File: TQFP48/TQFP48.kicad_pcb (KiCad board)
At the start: 2 copper layers, 61.2 x 18 mm, 11 parts, among them J1 Conn_01x24, J2 Conn_02x24_Counter_Clockwise, J3 Conn_02x24_Counter_Clockwise, J4 Conn_01x24, J5 Conn_01x05

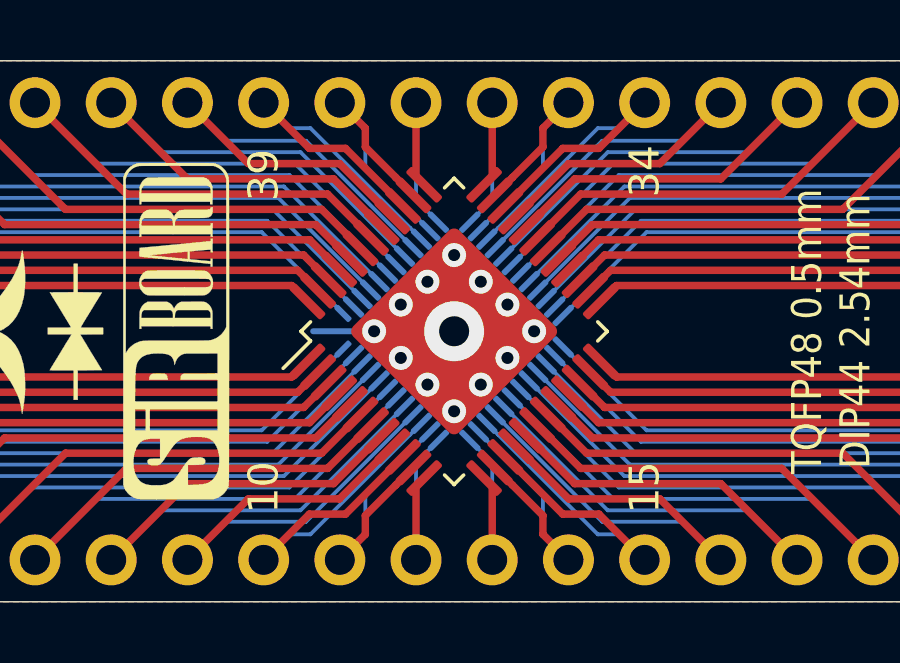
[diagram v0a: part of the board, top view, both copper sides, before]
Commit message: Silkscreens and sizes updated
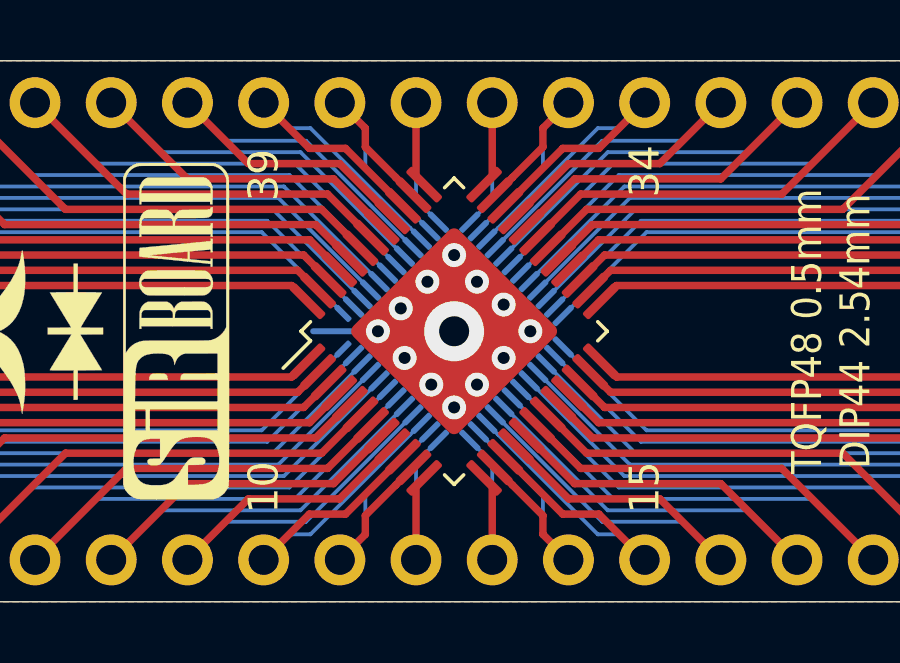
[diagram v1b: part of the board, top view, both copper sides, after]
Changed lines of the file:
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@@
   (page A4)
   (layers
-    (0 F.Cu signal hide)
-    (31 B.Cu signal hide)
+    (0 F.Cu signal)
+    (31 B.Cu signal)
     (32 B.Adhes user hide)
     (33 F.Adhes user hide)
@@
     (35 F.Paste user hide)
     (36 B.SilkS user)
-    (37 F.SilkS user hide)
-    (38 B.Mask user)
+    (37 F.SilkS user)
+    (38 B.Mask user hide)
     (39 F.Mask user hide)
     (40 Dwgs.User user hide)
@@
   )
   (module Package_QFP:TQFP-48-1EP_7x7mm_P0.5mm_EP5x5mm (layer F.Cu)
-    (at 148.59 104.145117 45)
+    (at 148.59 104.14 45)
     (descr "TQFP, 48 Pin (https://www.trinamic.com/fileadmin/assets/Products/ICs_Documents/TMC2100_datasheet_Rev1.08.pdf (page 45)), generated with kicad-footprint-generator ipc_qfp_generator.py")
     (tags "TQFP QFP")
@@
     (effects (font (size 1 1) (thickness 0.15)))
   )
-  (gr_circle (center 149.479833 102.49) (end 149.78 102.49) (layer B.Mask) (width 0.2))
-  (gr_circle (center 149.48 102.49) (end 149.780167 102.49) (layer F.Mask) (width 0.2))
-  (gr_circle (center 150.369833 103.25) (end 150.67 103.25) (layer B.Mask) (width 0.2))
-  (gr_circle (center 150.37 103.25) (end 150.670167 103.25) (layer F.Mask) (width 0.2))
-  (gr_circle (center 151.259833 104.14) (end 151.56 104.14) (layer B.Mask) (width 0.2))
-  (gr_circle (center 151.26 104.14) (end 151.560167 104.14) (layer F.Mask) (width 0.2))
-  (gr_circle (center 150.369833 105.03) (end 150.67 105.03) (layer B.Mask) (width 0.2))
-  (gr_circle (center 150.37 105.03) (end 150.670167 105.03) (layer F.Mask) (width 0.2))
-  (gr_circle (center 149.479833 105.92) (end 149.78 105.92) (layer B.Mask) (width 0.2))
-  (gr_circle (center 149.48 105.92) (end 149.780167 105.92) (layer F.Mask) (width 0.2))
-  (gr_circle (center 148.589833 106.81) (end 148.89 106.81) (layer B.Mask) (width 0.2))
-  (gr_circle (center 148.59 106.81) (end 148.890167 106.81) (layer F.Mask) (width 0.2))
-  (gr_circle (center 147.699833 105.92) (end 148 105.92) (layer B.Mask) (width 0.2))
-  (gr_circle (center 147.7 105.92) (end 148.000167 105.92) (layer F.Mask) (width 0.2))
-  (gr_circle (center 146.809833 105.03) (end 147.11 105.03) (layer B.Mask) (width 0.2))
-  (gr_circle (center 146.81 105.03) (end 147.110167 105.03) (layer F.Mask) (width 0.2))
-  (gr_circle (center 145.919833 104.14) (end 146.22 104.14) (layer B.Mask) (width 0.2))
-  (gr_circle (center 145.92 104.14) (end 146.220167 104.14) (layer F.Mask) (width 0.2))
-  (gr_circle (center 146.809833 103.25) (end 147.11 103.25) (layer B.Mask) (width 0.2))
-  (gr_circle (center 146.81 103.25) (end 147.110167 103.25) (layer F.Mask) (width 0.2))
+  (gr_circle (center 149.352 102.49) (end 149.652167 102.49) (layer B.Mask) (width 0.2))
+  (gr_circle (center 149.352 102.489) (end 149.652167 102.489) (layer F.Mask) (width 0.2))
+  (gr_circle (center 150.241 103.251) (end 150.541167 103.251) (layer B.Mask) (width 0.2))
+  (gr_circle (center 150.241 103.251) (end 150.541167 103.251) (layer F.Mask) (width 0.2))
+  (gr_circle (center 151.13 104.14) (end 151.430167 104.14) (layer B.Mask) (width 0.2))
+  (gr_circle (center 151.13 104.14) (end 151.430167 104.14) (layer F.Mask) (width 0.2))
+  (gr_circle (center 150.241 105.03) (end 150.541167 105.03) (layer B.Mask) (width 0.2))
+  (gr_circle (center 150.241 105.03) (end 150.541167 105.03) (layer F.Mask) (width 0.2))
+  (gr_circle (center 149.352 105.918) (end 149.652167 105.918) (layer B.Mask) (width 0.2))
+  (gr_circle (center 149.352 105.92) (end 149.652167 105.92) (layer F.Mask) (width 0.2))
+  (gr_circle (center 148.59 106.68) (end 148.890167 106.68) (layer B.Mask) (width 0.2))
+  (gr_circle (center 148.59 106.68) (end 148.890167 106.68) (layer F.Mask) (width 0.2))
+  (gr_circle (center 147.828 105.92) (end 148.128167 105.92) (layer B.Mask) (width 0.2))
+  (gr_circle (center 147.828 105.918) (end 148.128167 105.918) (layer F.Mask) (width 0.2))
+  (gr_circle (center 146.939 105.029) (end 147.239167 105.029) (layer B.Mask) (width 0.2))
+  (gr_circle (center 146.939 105.029) (end 147.239167 105.029) (layer F.Mask) (width 0.2))
+  (gr_circle (center 146.05 104.14) (end 146.350167 104.14) (layer B.Mask) (width 0.2))
+  (gr_circle (center 146.05 104.14) (end 146.350167 104.14) (layer F.Mask) (width 0.2))
+  (gr_circle (center 146.809833 103.378) (end 147.11 103.378) (layer B.Mask) (width 0.2))
+  (gr_circle (center 146.81 103.378) (end 147.110167 103.378) (layer F.Mask) (width 0.2))
   (gr_circle (center 147.699833 102.49) (end 148 102.49) (layer B.Mask) (width 0.2))
   (gr_circle (center 147.7 102.49) (end 148.000167 102.49) (layer F.Mask) (width 0.2))
@@
   (segment (start 173.482 100.838) (end 176.674151 97.645849) (width 0.127) (layer B.Cu) (net 48))
   (via (at 148.59 104.14) (size 2) (drill 1) (layers F.Cu B.Cu) (net 49))
-  (via (at 145.923 104.14) (size 0.8) (drill 0.4) (layers F.Cu B.Cu) (net 49))
-  (via (at 146.812 103.251) (size 0.8) (drill 0.4) (layers F.Cu B.Cu) (net 49))
-  (via (at 146.812 105.029) (size 0.8) (drill 0.4) (layers F.Cu B.Cu) (net 49))
-  (via (at 150.368 105.029) (size 0.8) (drill 0.4) (layers F.Cu B.Cu) (net 49))
-  (via (at 150.368 103.251) (size 0.8) (drill 0.4) (layers F.Cu B.Cu) (net 49))
+  (via (at 146.05 104.14) (size 0.8) (drill 0.4) (layers F.Cu B.Cu) (net 49))
+  (via (at 146.812 103.378) (size 0.8) (drill 0.4) (layers F.Cu B.Cu) (net 49))
+  (via (at 146.939 105.029) (size 0.8) (drill 0.4) (layers F.Cu B.Cu) (net 49))
+  (via (at 150.241 105.029) (size 0.8) (drill 0.4) (layers F.Cu B.Cu) (net 49))
+  (via (at 150.241 103.251) (size 0.8) (drill 0.4) (layers F.Cu B.Cu) (net 49))
   (via (at 147.701 102.489) (size 0.8) (drill 0.4) (layers F.Cu B.Cu) (net 49))
-  (via (at 149.479 102.489) (size 0.8) (drill 0.4) (layers F.Cu B.Cu) (net 49))
-  (via (at 147.701 105.918) (size 0.8) (drill 0.4) (layers F.Cu B.Cu) (net 49))
-  (via (at 149.479 105.918) (size 0.8) (drill 0.4) (layers F.Cu B.Cu) (net 49))
-  (via (at 148.59 106.807) (size 0.8) (drill 0.4) (layers F.Cu B.Cu) (net 49))
+  (via (at 149.352 102.489) (size 0.8) (drill 0.4) (layers F.Cu B.Cu) (net 49))
+  (via (at 147.828 105.918) (size 0.8) (drill 0.4) (layers F.Cu B.Cu) (net 49))
+  (via (at 149.352 105.918) (size 0.8) (drill 0.4) (layers F.Cu B.Cu) (net 49))
+  (via (at 148.59 106.68) (size 0.8) (drill 0.4) (layers F.Cu B.Cu) (net 49))
   (via (at 148.59 101.6) (size 0.8) (drill 0.4) (layers F.Cu B.Cu) (net 49))
-  (via (at 151.257 104.14) (size 0.8) (drill 0.4) (layers F.Cu B.Cu) (net 49))
+  (via (at 151.13 104.14) (size 0.8) (drill 0.4) (layers F.Cu B.Cu) (net 49))
   (segment (start 148.59 104.14) (end 143.891 104.14) (width 0.2) (layer B.Cu) (net 49))
   (zone (net 49) (net_name "Net-(J5-Pad1)") (layer B.Cu) (hatch none 0.508)

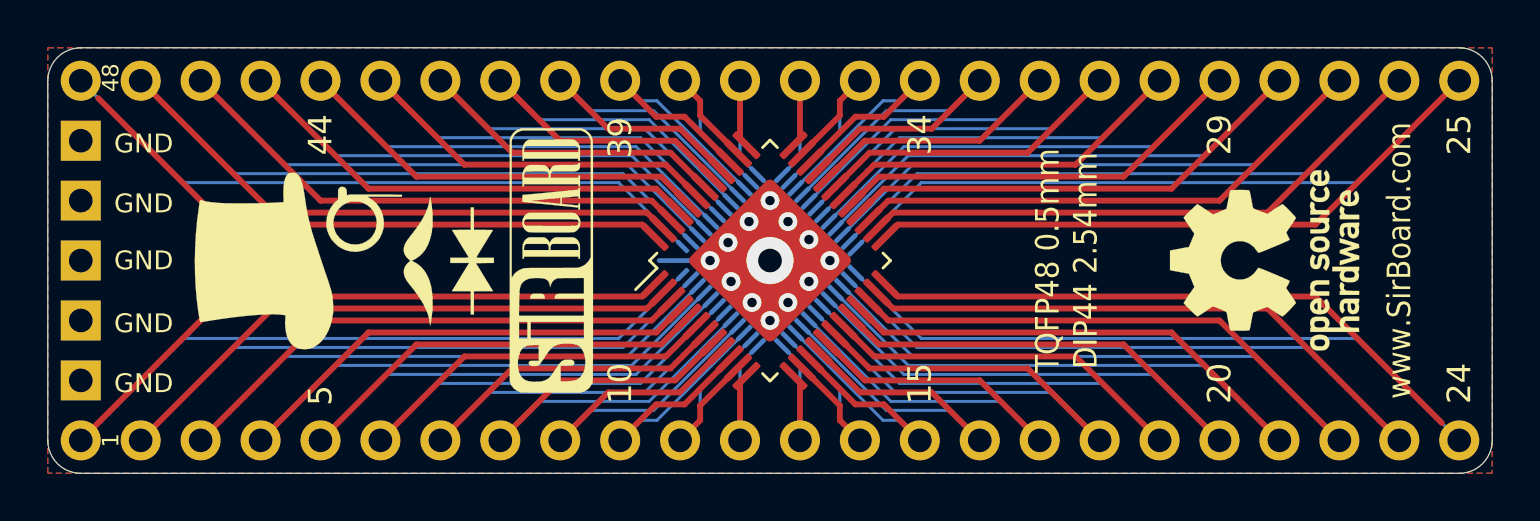
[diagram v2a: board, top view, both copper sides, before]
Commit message: Pin Numbering edited
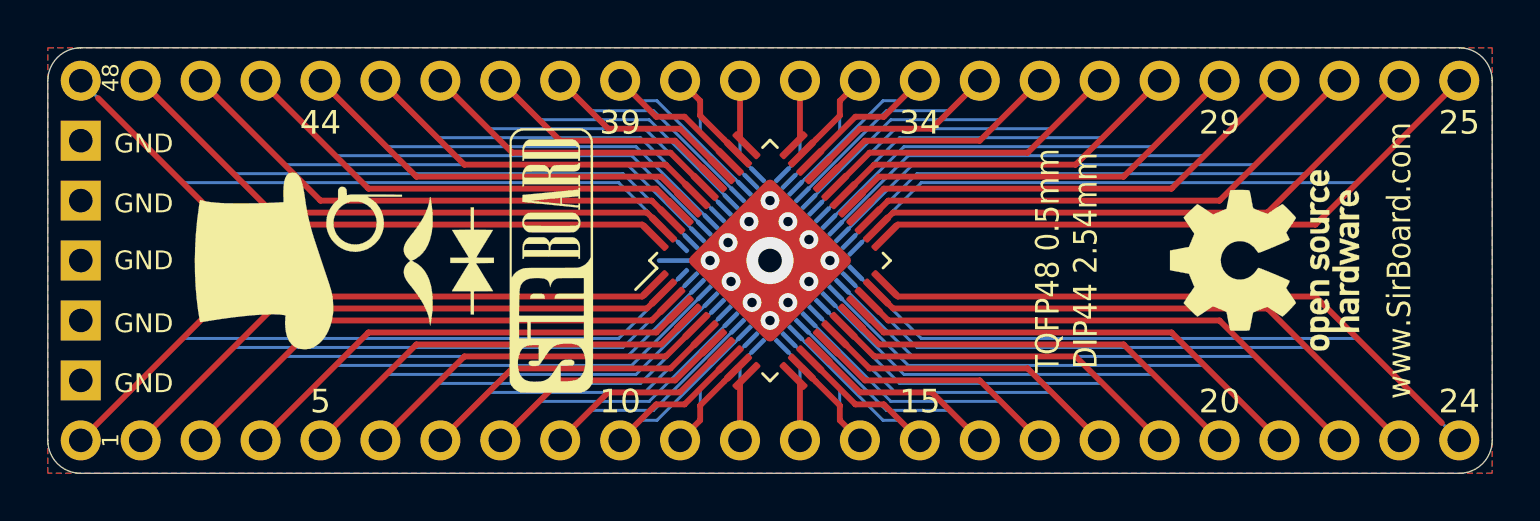
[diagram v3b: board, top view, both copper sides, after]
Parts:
- J1, J4, J5: moved to F.Cu
- turned J1 to 90 degrees
- turned J4 to 90 degrees
- turned J5 to 0 degrees

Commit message: Numbering Orientation Edited
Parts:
- J1, J4, J5: moved to B.Cu
- turned J1 to 270 degrees
- turned J4 to 270 degrees
- turned J5 to 180 degrees

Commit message: Silkscreen Edits
Dimensions moved to Drawings Layer
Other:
- rule pad_to_mask_clearance: 0.051 -> 0
- rule solder_mask_min_width: 0.25 -> 0.1
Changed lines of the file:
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@@
     (pad_size 5 5)
     (pad_drill 0)
-    (pad_to_mask_clearance 0.051)
-    (solder_mask_min_width 0.25)
+    (pad_to_mask_clearance 0)
+    (solder_mask_min_width 0.1)
     (aux_axis_origin 0 0)
     (visible_elements 7FFFFFFF)
     (pcbplotparams
-      (layerselection 0x010fc_ffffffff)
+      (layerselection 0x010f0_ffffffff)
       (usegerberextensions false)
       (usegerberattributes false)
@@
       (linewidth 0.100000)
       (plotframeref false)
-      (viasonmask false)
+      (viasonmask true)
       (mode 1)
-      (useauxorigin false)
+      (useauxorigin true)
       (hpglpennumber 1)
       (hpglpenspeed 20)
@@
       (psa4output false)
       (plotreference true)
-      (plotvalue true)
+      (plotvalue false)
       (plotinvisibletext false)
       (padsonsilk false)
@@
       (outputformat 1)
       (mirror false)
-      (drillshape 1)
+      (drillshape 0)
       (scaleselection 1)
-      (outputdirectory ""))
+      (outputdirectory "../../Gerbers/TQFP48/"))
   )
   (net 0 "")
@@
       (xy 0.500964 -3.601424)) (layer F.SilkS) (width 0.01))
   )
-  (dimension 18.034 (width 0.15) (layer F.SilkS)
-    (gr_text "18.034 mm" (at 111.349 104.14 270) (layer F.SilkS)
+  (dimension 18.034 (width 0.15) (layer Dwgs.User)
+    (gr_text "18.034 mm" (at 111.349 104.14 270) (layer Dwgs.User)
       (effects (font (size 1 1) (thickness 0.15)) hide)
     )
@@
     (arrow2b (pts (xy 112.649 95.123) (xy 113.235421 96.249504)))
   )
-  (dimension 15.24 (width 0.15) (layer F.SilkS)
-    (gr_text "15.240 mm" (at 114.524 104.14 270) (layer F.SilkS)
+  (dimension 15.24 (width 0.15) (layer Dwgs.User)
+    (gr_text "15.240 mm" (at 114.524 104.14 270) (layer Dwgs.User)
       (effects (font (size 1 1) (thickness 0.15)) hide)
     )
@@
     (arrow2b (pts (xy 115.824 96.52) (xy 116.410421 97.646504)))
   )
-  (dimension 58.42 (width 0.15) (layer F.SilkS)
-    (gr_text "58.420 mm" (at 148.59 91.791) (layer F.SilkS)
+  (dimension 58.42 (width 0.15) (layer Dwgs.User)
+    (gr_text "58.420 mm" (at 148.59 91.791) (layer Dwgs.User)
       (effects (font (size 1 1) (thickness 0.15)) hide)
     )
@@
     (arrow2b (pts (xy 119.38 93.091) (xy 120.506504 92.504579)))
   )
-  (dimension 61.214 (width 0.15) (layer F.SilkS)
-    (gr_text "61.214 mm" (at 148.59 89.378) (layer F.SilkS)
+  (dimension 61.214 (width 0.15) (layer Dwgs.User)
+    (gr_text "61.214 mm" (at 148.59 89.378) (layer Dwgs.User)
       (effects (font (size 1 1) (thickness 0.15)) hide)
     )

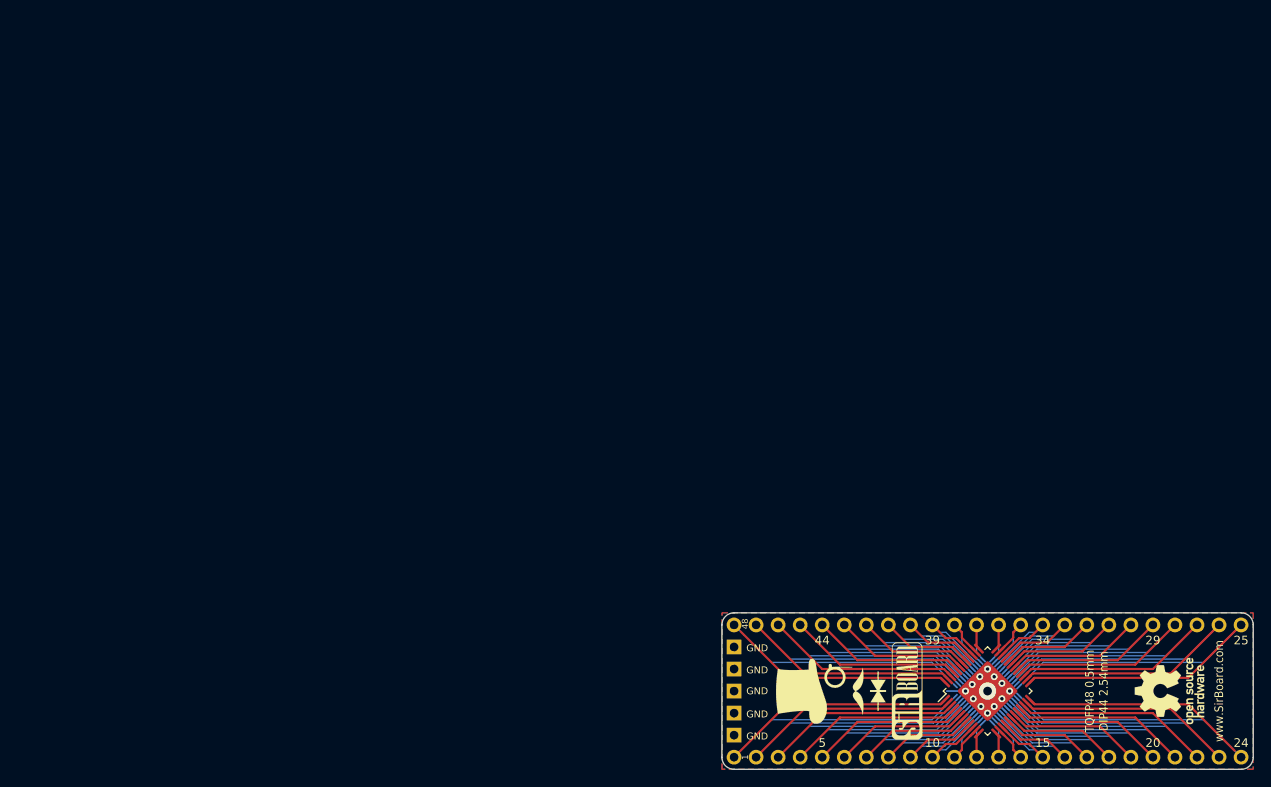
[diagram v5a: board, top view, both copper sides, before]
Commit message: USB, SD and CR Cells Added
MicroSD, MicroUSB, MiniUSB, USB-C, CR1220, CR2032 added as well as all schematics page sizes optimised
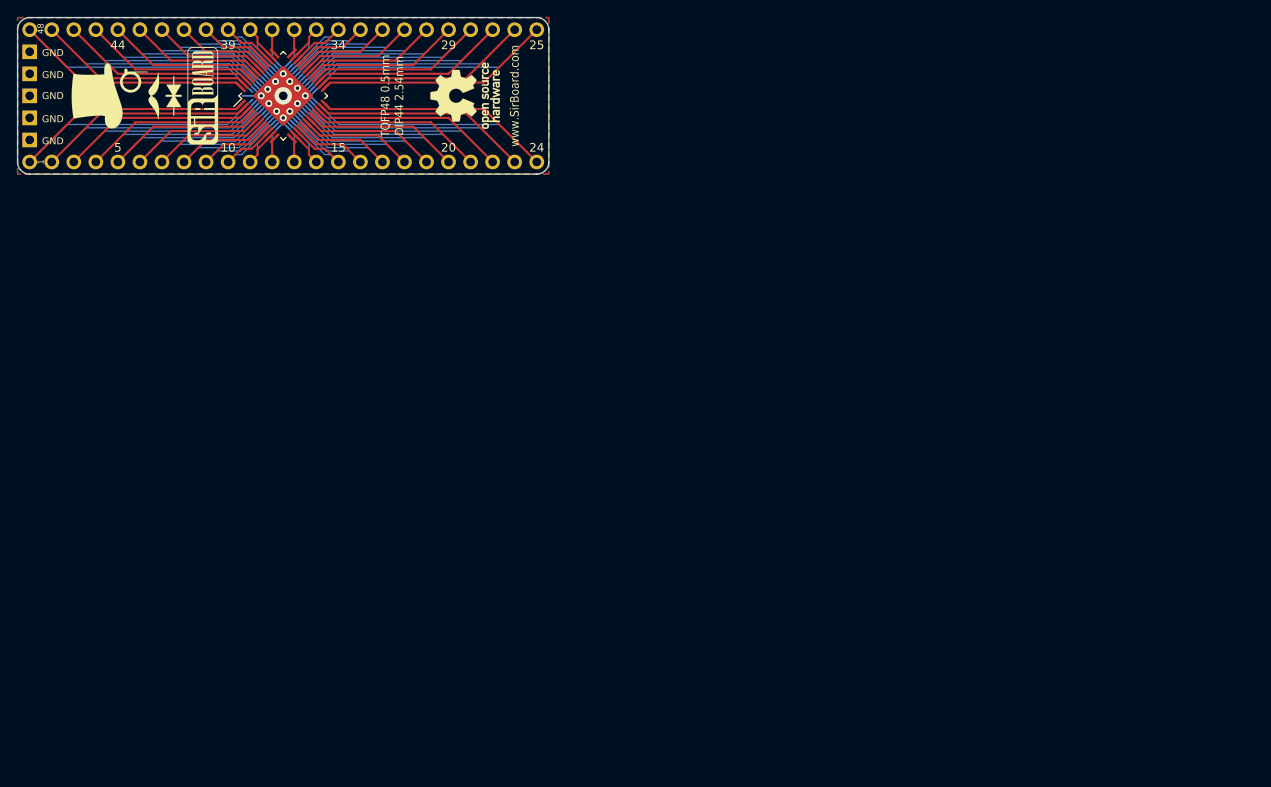
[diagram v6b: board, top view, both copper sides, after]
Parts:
- moved G*** 106.2 mm to (79.0, 35.6)
- moved G*** 106.2 mm to (88.4, 35.6)
- moved G*** 106.2 mm to (58.2, 35.6)
- moved G*** 106.2 mm to (49.4, 35.6)
- moved J1 106.2 mm to (38.2, 43.2)
- moved J2 106.2 mm to (67.4, 35.6)
- moved J3 106.2 mm to (67.4, 35.6)
- moved J4 106.2 mm to (38.2, 27.9)
- moved J5 106.2 mm to (38.2, 30.5)
- moved REF** 106.2 mm to (50.8, 35.6)
- moved REF** 106.2 mm to (88.4, 35.6)
